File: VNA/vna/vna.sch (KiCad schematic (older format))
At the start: 2 parts, among them J1 Conn_Coaxial, J2 Conn_Coaxial

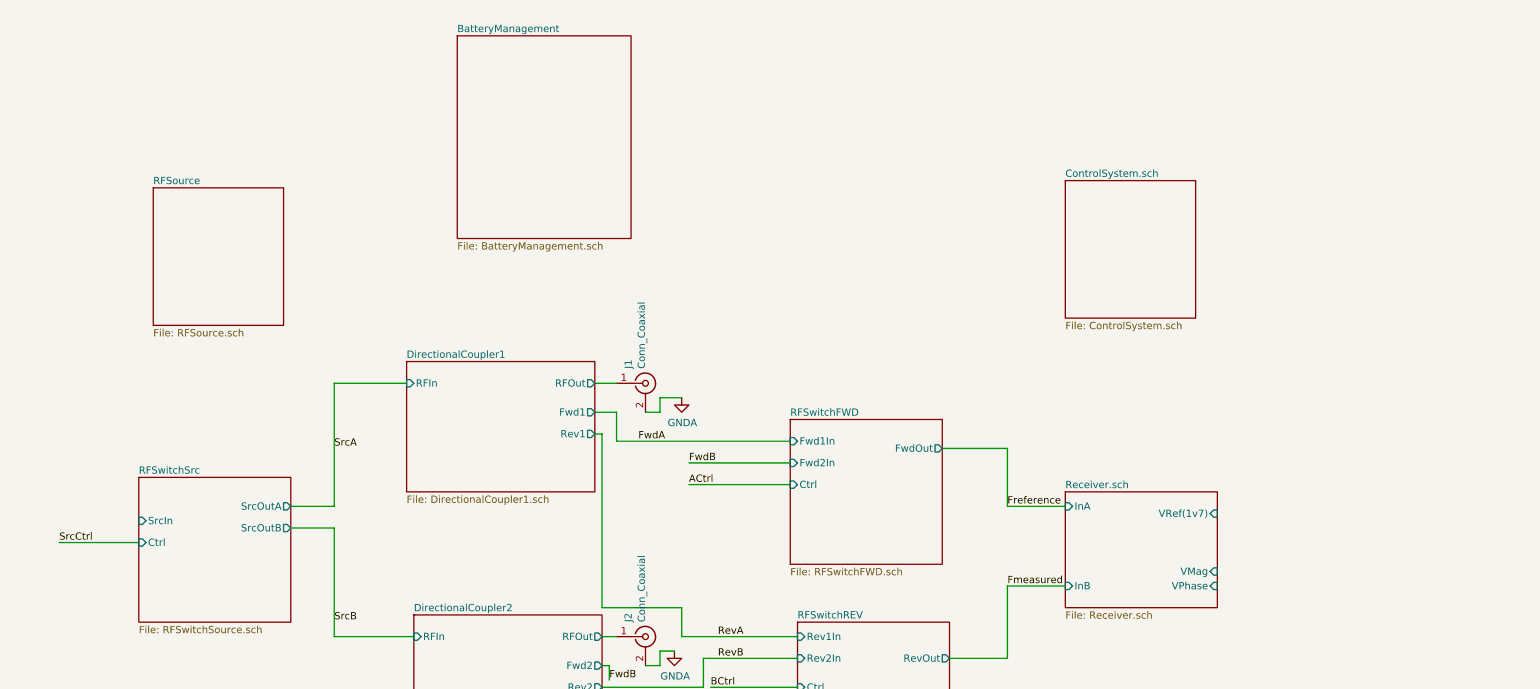
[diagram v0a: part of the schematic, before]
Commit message: block diagram for presentation completed
at this stage i have completed the overall block diagram for the initial presentation.

the blocks are mostly empty and require further development. the overall block diagram neglects power supply connections for clarity, these will be added internal to the blocks.
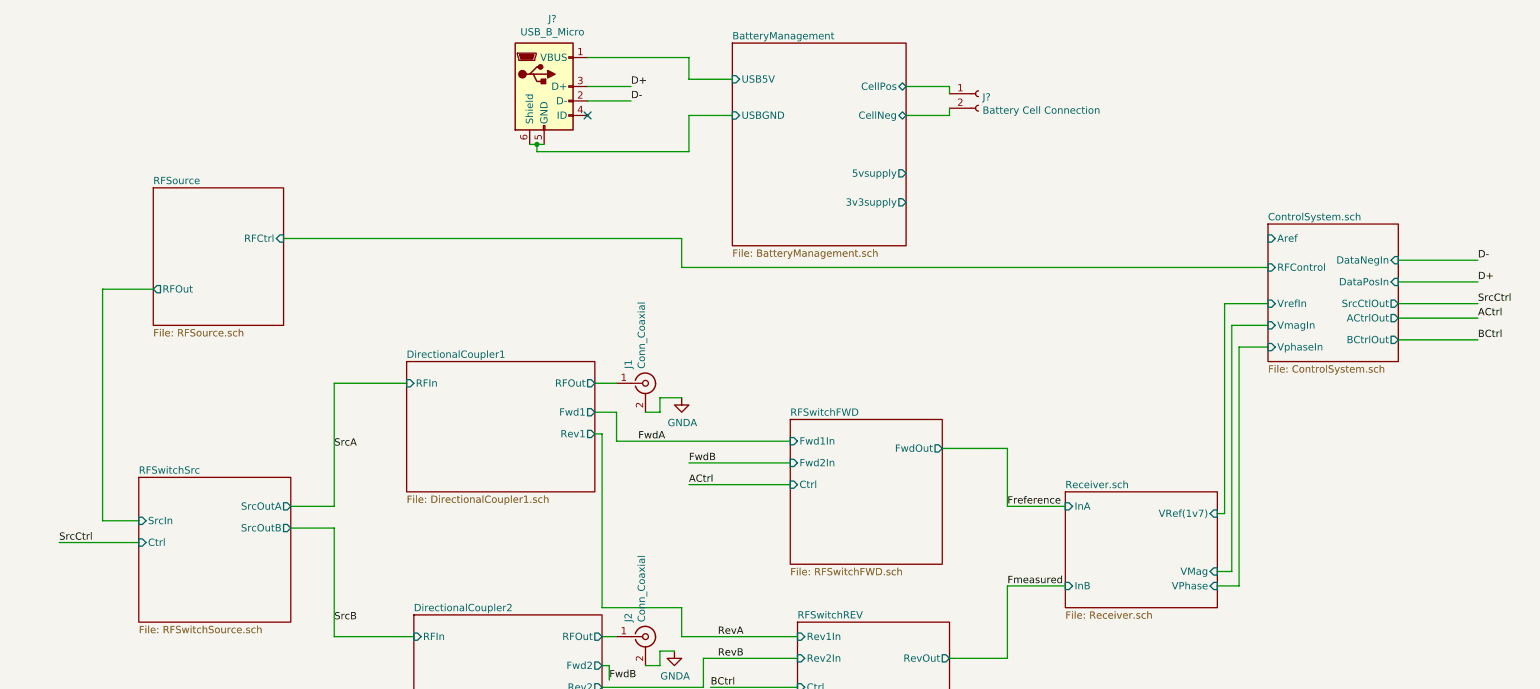
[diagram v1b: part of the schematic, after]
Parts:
- added J?: USB_B_Micro, symbol Connector:USB_B_Micro
- added J?: Battery Cell Connection, symbol Connector:Conn_01x02_Female
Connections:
- new net BatteryManagement/CellNeg: J?.2 (Pin_2)
- new net BatteryManagement/CellPos: J?.1 (Pin_1)
- new net BatteryManagement/USB5V: J?.1 (VBUS)
- new net BatteryManagement/USBGND: J?.5 (GND), J?.6 (Shield)
- new net D+: J?.3 (D+)
- new net D-: J?.2 (D-)
- no-connect marks 0 -> 1
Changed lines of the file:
@@
 $Descr A4 11693 8268
 encoding utf-8
-Sheet 1 9
+Sheet 1 10
 Title "Vector Network Analyser"
 Date "2019-04-24"
@@
 BCtrl
 $Sheet
-S 8100 2000 900  950
-U 5CD1CF30
-F0 "ControlSystem.sch" 50
-F1 "ControlSystem.sch" 50
-$EndSheet
-$Sheet
 S 1800 2050 900  950
 U 5CDF14FF
 F0 "RFSource" 50
 F1 "RFSource.sch" 50
-$EndSheet
-$Sheet
-S 3900 1000 1200 1400
+F2 "RFOut" O L 1800 2750 50
+F3 "RFCtrl" I R 2700 2400 50
+$EndSheet
+$Sheet
+S 5800 1050 1200 1400
 U 5CDF1C56
 F0 "BatteryManagement" 50
 F1 "BatteryManagement.sch" 50
-$EndSheet
+F2 "USB5V" I L 5800 1300 50
+F3 "USBGND" I L 5800 1550 50
+F4 "3v3supply" O R 7000 2150 50
+F5 "5vsupply" O R 7000 1950 50
+F6 "CellPos" B R 7000 1350 50
+F7 "CellNeg" B R 7000 1550 50
+$EndSheet
+$Comp
+L Connector:USB_B_Micro J?
+U 1 1 5CE2753D
+P 4500 1350
+F 0 "J?" H 4557 1817 50  0000 C CNN
+F 1 "USB_B_Micro" H 4557 1726 50  0000 C CNN
+F 2 "" H 4650 1300 50  0001 C CNN
+F 3 "~" H 4650 1300 50  0001 C CNN
+	1    4500 1350
+	1    0    0    -1
+$EndComp
+Wire Wire Line
+	4800 1150 5500 1150
+Wire Wire Line
+	5500 1150 5500 1300
+Wire Wire Line
+	5500 1300 5800 1300
+Wire Wire Line
+	4400 1750 4450 1750
+Wire Wire Line
+	4450 1750 4450 1800
+Wire Wire Line
+	4450 1800 5500 1800
+Wire Wire Line
+	5500 1800 5500 1550
+Wire Wire Line
+	5500 1550 5800 1550
+Connection ~ 4450 1750
+Wire Wire Line
+	4450 1750 4500 1750
+$Sheet
+S 9500 2300 900  950
+U 5CD1CF30
+F0 "ControlSystem.sch" 50
+F1 "ControlSystem.sch" 50
+F2 "Aref" I L 9500 2400 50
+F3 "VmagIn" I L 9500 3000 50
+F4 "VphaseIn" I L 9500 3150 50
+F5 "VrefIn" I L 9500 2850 50
+F6 "DataNegIn" I R 10400 2550 50
+F7 "DataPosIn" I R 10400 2700 50
+F8 "SrcCtlOut" O R 10400 2850 50
+F9 "ACtrlOut" O R 10400 2950 50
+F10 "BCtrlOut" O R 10400 3100 50
+F11 "RFControl" I L 9500 2600 50
+$EndSheet
+Wire Wire Line
+	9150 4300 9200 4300
+Wire Wire Line
+	9200 4300 9200 2850
+Wire Wire Line
+	9200 2850 9500 2850
+Wire Wire Line
+	9150 4700 9250 4700
+Wire Wire Line
+	9250 4700 9250 3000
+Wire Wire Line
+	9250 3000 9500 3000
+Wire Wire Line
+	9150 4800 9300 4800
+Wire Wire Line
+	9300 4800 9300 3150
+Wire Wire Line
+	9300 3150 9500 3150
+Wire Wire Line
+	10400 2550 10950 2550
+Wire Wire Line
+	10400 2700 10950 2700
+Text Label 10950 2550 0    50   ~ 0
+D-
+Text Label 10950 2700 0    50   ~ 0
+D+
+NoConn ~ 4800 1550
+Wire Wire Line
+	4800 1350 5100 1350
+Wire Wire Line
+	4800 1450 5100 1450
+Text Label 5100 1350 0    50   ~ 0
+D+
+Text Label 5100 1450 0    50   ~ 0
+D-
+Wire Wire Line
+	10400 2850 10950 2850
+Wire Wire Line
+	10400 2950 10950 2950
+Wire Wire Line
+	10400 3100 10950 3100
+Text Label 10950 2850 0    50   ~ 0
+SrcCtrl
+Text Label 10950 2950 0    50   ~ 0
+ACtrl
+Text Label 10950 3100 0    50   ~ 0
+BCtrl
+$Comp
+L Connector:Conn_01x02_Female J?
+U 1 1 5CE4F062
+P 7500 1400
+F 0 "J?" H 7528 1376 50  0000 L CNN
+F 1 "Battery Cell Connection" H 7528 1285 50  0000 L CNN
+F 2 "" H 7500 1400 50  0001 C CNN
+F 3 "~" H 7500 1400 50  0001 C CNN
+	1    7500 1400
+	1    0    0    -1
+$EndComp
+Wire Wire Line
+	7000 1350 7300 1350
+Wire Wire Line
+	7300 1350 7300 1400
+Wire Wire Line
+	7000 1550 7300 1550
+Wire Wire Line
+	7300 1550 7300 1500
+Wire Wire Line
+	1700 4350 1450 4350
+Wire Wire Line
+	1450 4350 1450 2750
+Wire Wire Line
+	1450 2750 1800 2750
+Wire Wire Line
+	2700 2400 5450 2400
+Wire Wire Line
+	5450 2400 5450 2600
+Wire Wire Line
+	5450 2600 9500 2600
 $EndSCHEMATC

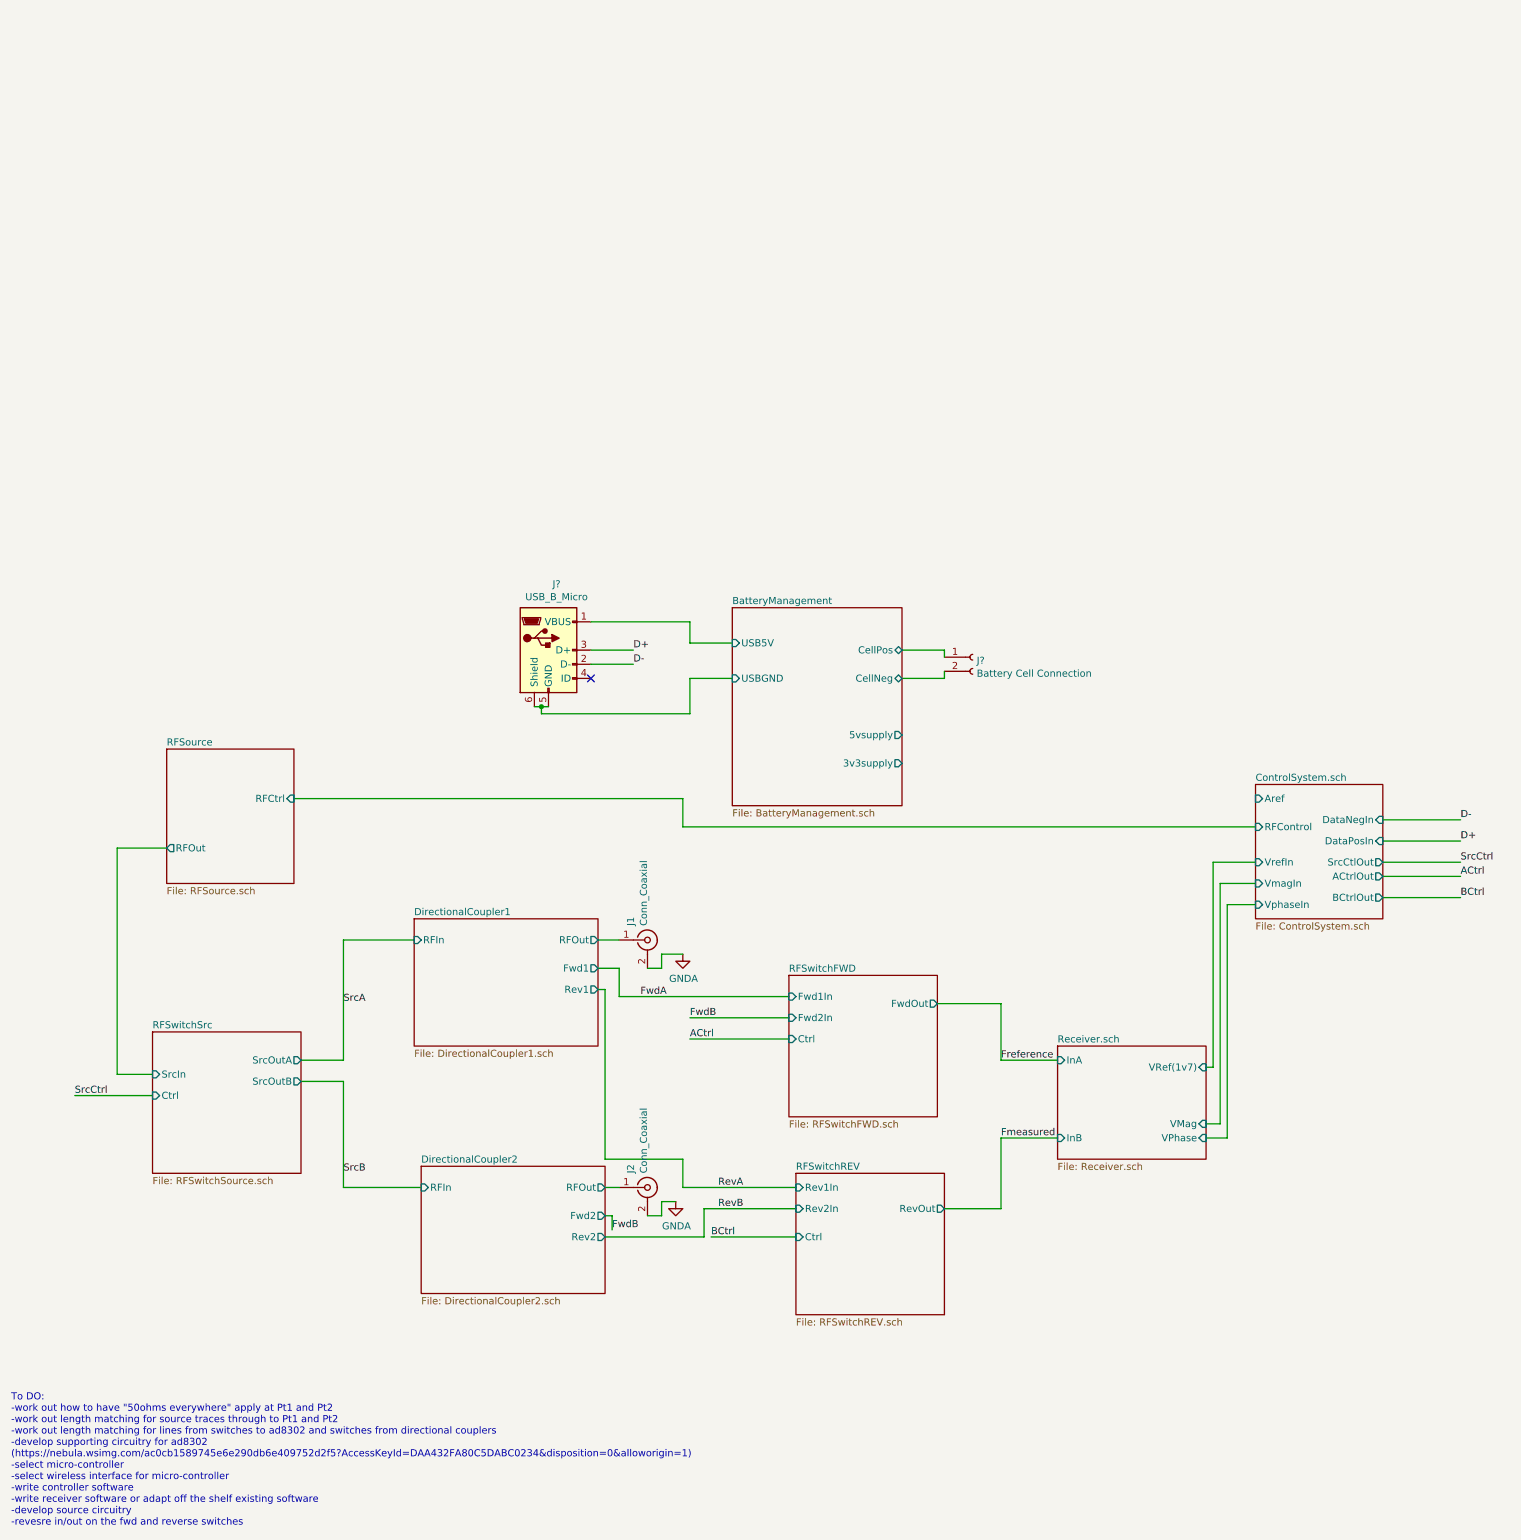
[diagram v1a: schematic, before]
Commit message: adjusted main schematic to suit initial presentation
i moved a few blocks around so that the cropped version of the block diagram would fit nicely in my semester 1 presentation
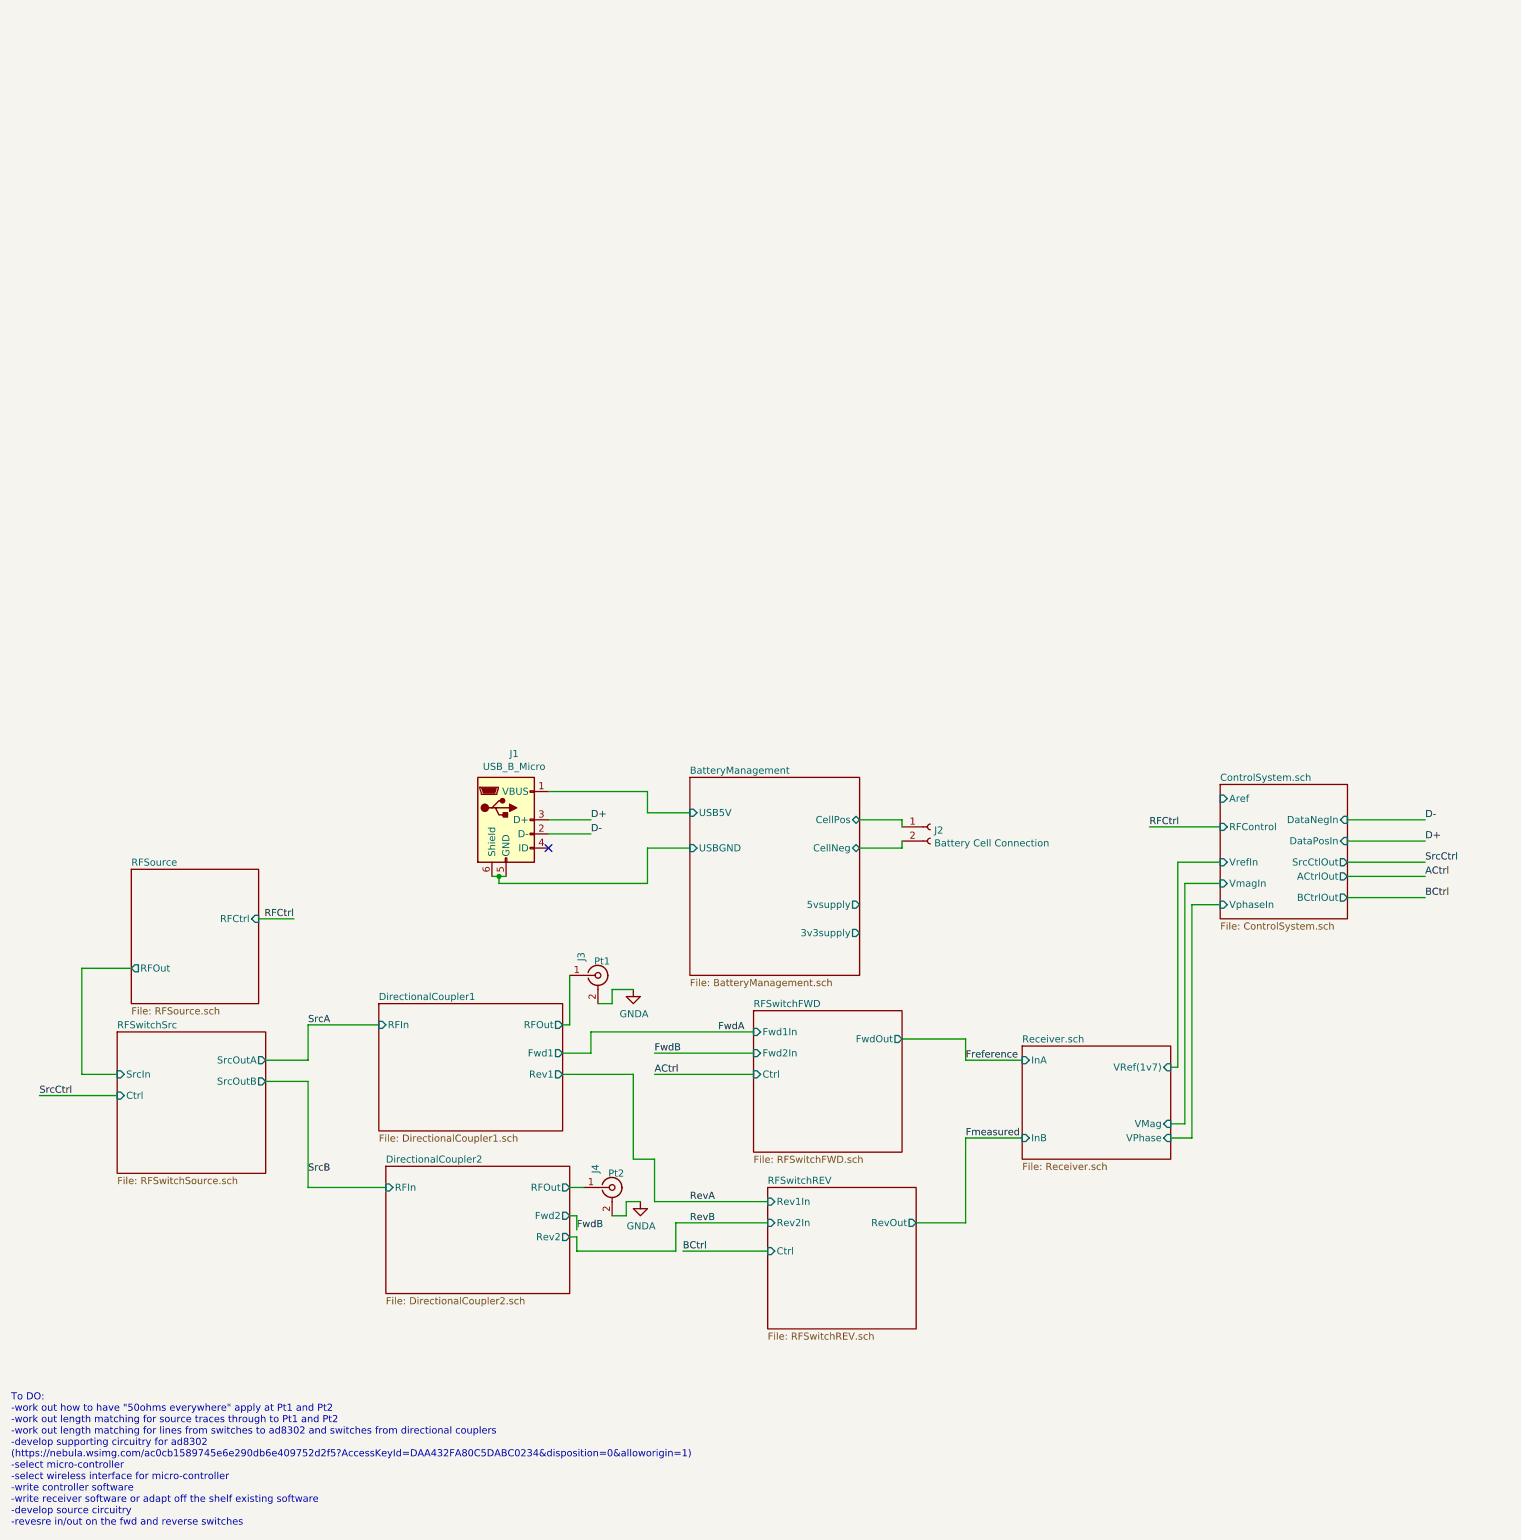
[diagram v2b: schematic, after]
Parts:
- J3: renamed from J1; value Conn_Coaxial -> Pt1
- J4: renamed from J2; value Conn_Coaxial -> Pt2
- gave numbers to parts that had none: 2
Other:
- moved on the sheet: J1, J2, J3, J4
